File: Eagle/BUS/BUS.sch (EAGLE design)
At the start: 10 parts

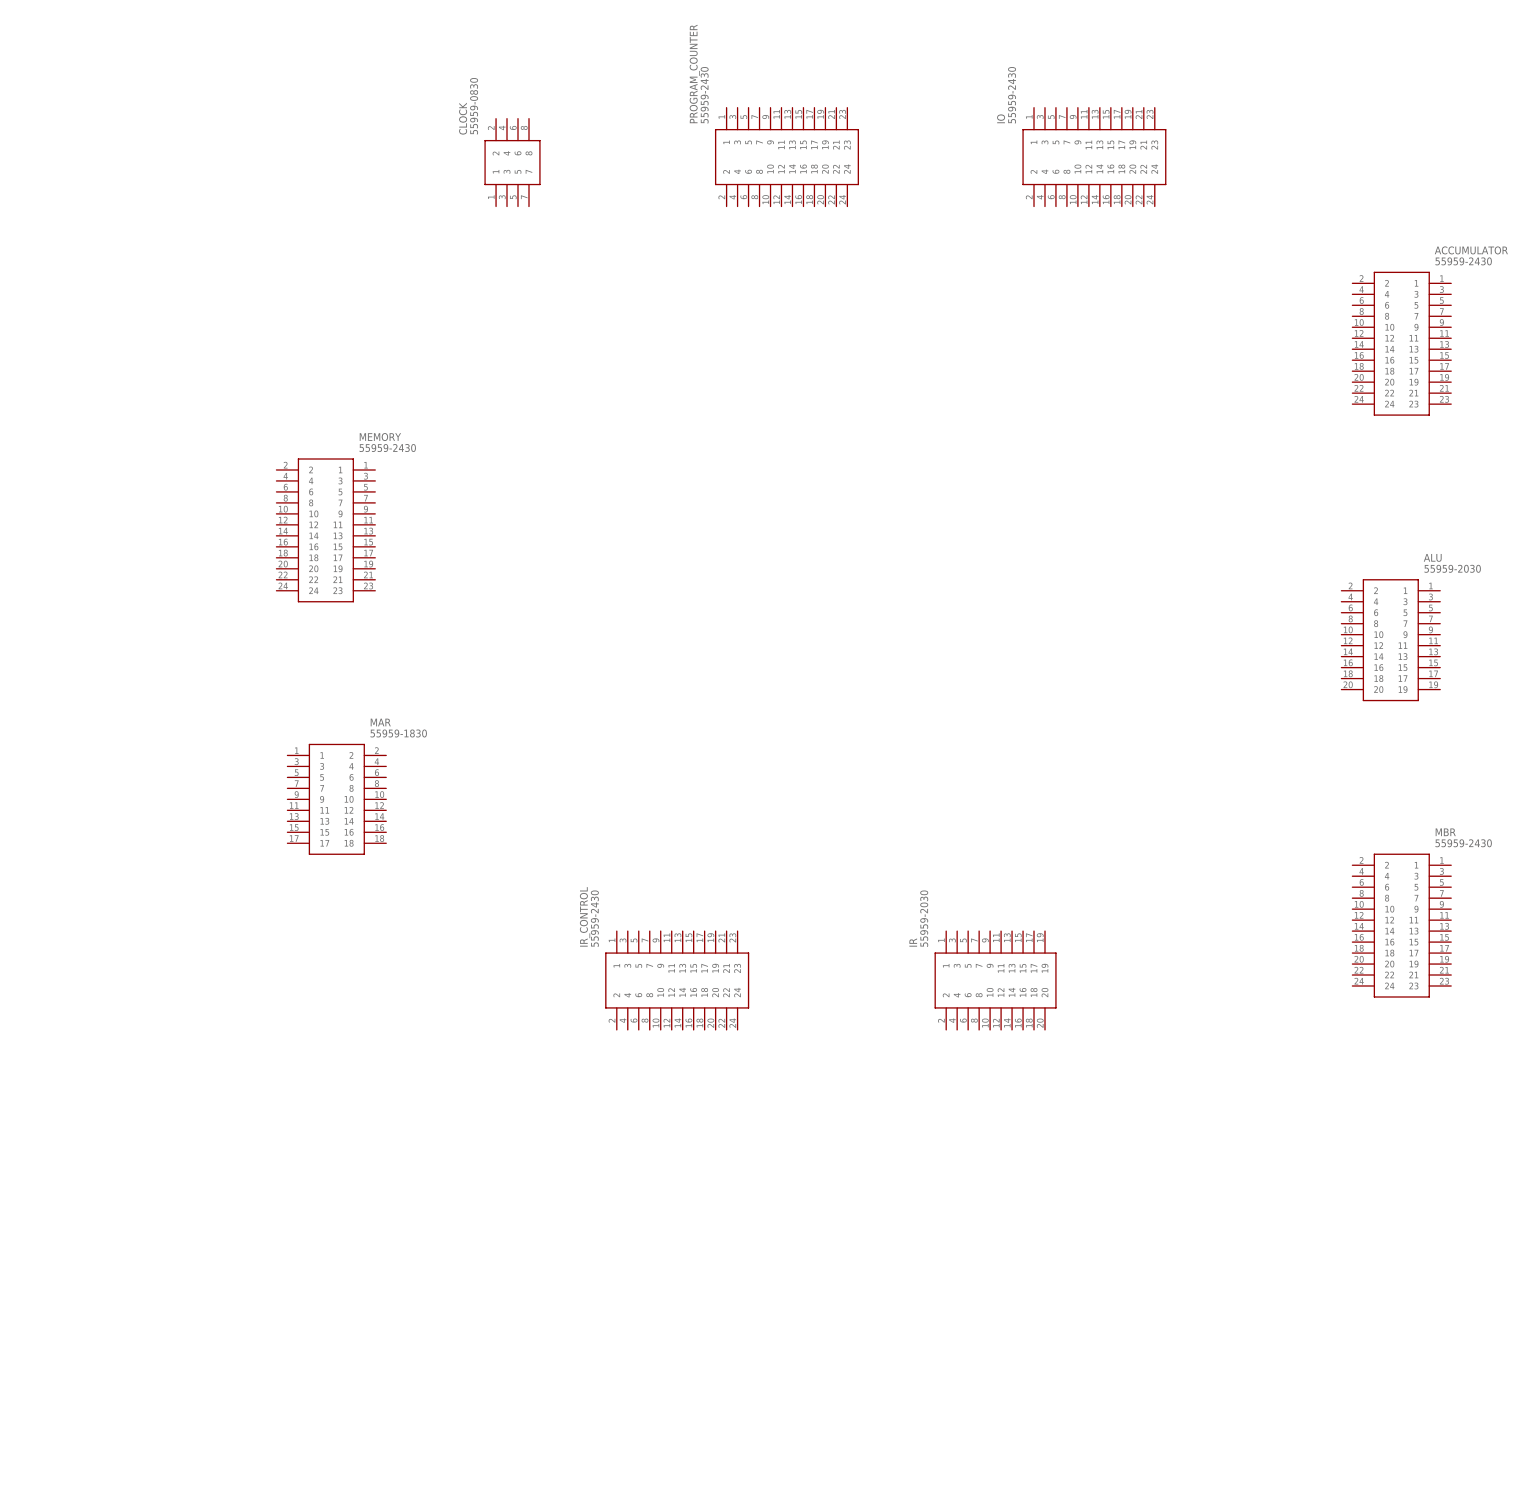
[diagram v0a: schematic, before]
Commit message: added BUS
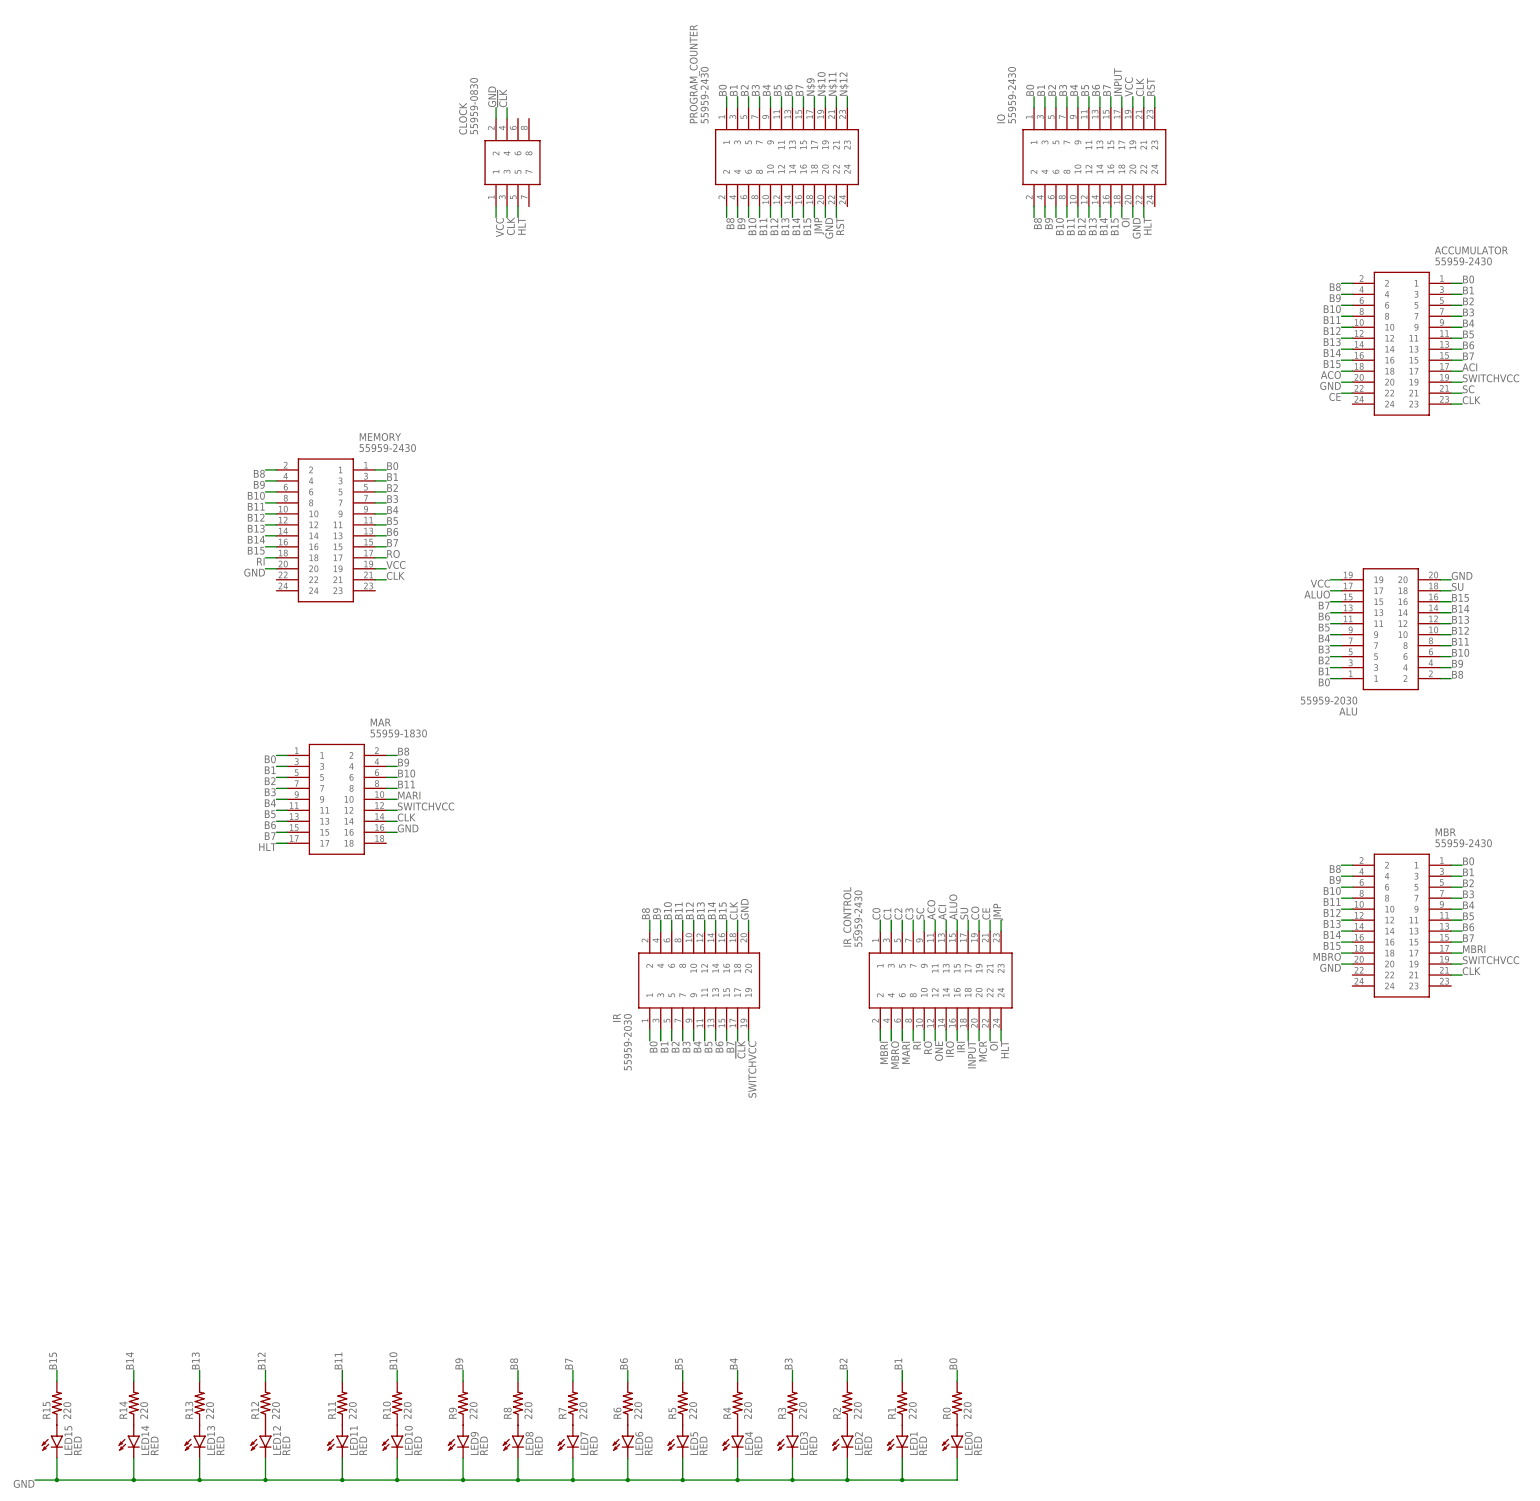
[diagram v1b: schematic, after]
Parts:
- added LED0, LED1, LED10, LED11, LED12, LED13, LED14, LED15, LED2, LED3, LED4, LED5, LED6, LED7, LED8, LED9: RED, led:LED3MM
- added R0, R1, R10, R11, R12, R13, R14, R15, R2, R3, R4, R5, R6, R7, R8, R9: 220, rcl:R-US_0204/7
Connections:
- new net !CLK: CLOCK.4, IR.17
- new net ACI: ACCUMULATOR.17, IR_CONTROL.13
- new net ACO: ACCUMULATOR.18, IR_CONTROL.11
- new net ALUO: ALU.17, IR_CONTROL.15
- new net B0: ACCUMULATOR.1, ALU.1, IO.1, IR.1, MAR.1, MBR.1, MEMORY.1, PROGRAM_COUNTER.1, R0.2
- new net B1: ACCUMULATOR.3, ALU.3, IO.3, IR.3, MAR.3, MBR.3, MEMORY.3, PROGRAM_COUNTER.3, R1.2
- new net B10: ACCUMULATOR.6, ALU.6, IO.6, IR.6, MAR.6, MBR.6, MEMORY.6, PROGRAM_COUNTER.6, R10.2
- new net B11: ACCUMULATOR.8, ALU.8, IO.8, IR.8, MAR.8, MBR.8, MEMORY.8, PROGRAM_COUNTER.8, R11.2
- new net B12: ACCUMULATOR.10, ALU.10, IO.10, IR.10, MBR.10, MEMORY.10, PROGRAM_COUNTER.10, R12.2
- new net B13: ACCUMULATOR.12, ALU.12, IO.12, IR.12, MBR.12, MEMORY.12, PROGRAM_COUNTER.12, R13.2
- new net B14: ACCUMULATOR.14, ALU.14, IO.14, IR.14, MBR.14, MEMORY.14, PROGRAM_COUNTER.14, R14.2
- new net B15: ACCUMULATOR.16, ALU.16, IO.16, IR.16, MBR.16, MEMORY.16, PROGRAM_COUNTER.16, R15.2
- new net B2: ACCUMULATOR.5, ALU.5, IO.5, IR.5, MAR.5, MBR.5, MEMORY.5, PROGRAM_COUNTER.5, R2.2
- new net B3: ACCUMULATOR.7, ALU.7, IO.7, IR.7, MAR.7, MBR.7, MEMORY.7, PROGRAM_COUNTER.7, R3.2
- new net B4: ACCUMULATOR.9, ALU.9, IO.9, IR.9, MAR.9, MBR.9, MEMORY.9, PROGRAM_COUNTER.9, R4.2
- new net B5: ACCUMULATOR.11, ALU.11, IO.11, IR.11, MAR.11, MBR.11, MEMORY.11, PROGRAM_COUNTER.11, R5.2
- new net B6: ACCUMULATOR.13, ALU.13, IO.13, IR.13, MAR.13, MBR.13, MEMORY.13, PROGRAM_COUNTER.13, R6.2
- new net B7: ACCUMULATOR.15, ALU.15, IO.15, IR.15, MAR.15, MBR.15, MEMORY.15, PROGRAM_COUNTER.15, R7.2
- new net B8: ACCUMULATOR.2, ALU.2, IO.2, IR.2, MAR.2, MBR.2, MEMORY.2, PROGRAM_COUNTER.2, R8.2
- new net B9: ACCUMULATOR.4, ALU.4, IO.4, IR.4, MAR.4, MBR.4, MEMORY.4, PROGRAM_COUNTER.4, R9.2
- new net C0: IR_CONTROL.1
- new net C1: IR_CONTROL.3
- new net C2: IR_CONTROL.5
- new net C3: IR_CONTROL.7
- new net CE: ACCUMULATOR.22, IR_CONTROL.21
- new net CLK: ACCUMULATOR.23, CLOCK.3, IO.21, IR.18, MAR.14, MBR.21, MEMORY.21
- new net CO: IR_CONTROL.19
- new net GND: ACCUMULATOR.20, ALU.20, CLOCK.2, IO.20, IR.20, LED0.C, LED1.C, LED10.C, LED11.C, LED12.C, LED13.C, LED14.C, LED15.C, LED2.C, LED3.C, LED4.C, LED5.C, LED6.C, LED7.C, LED8.C, LED9.C, MAR.16, MBR.20, MEMORY.20, PROGRAM_COUNTER.20
- new net HLT: CLOCK.5, IO.22, IR_CONTROL.24, MAR.17
- new net INPUT: IO.17, IR_CONTROL.18
- new net IRI: IR_CONTROL.16
- new net IRO: IR_CONTROL.14
- new net JMP: IR_CONTROL.23, PROGRAM_COUNTER.18
- new net MARI: IR_CONTROL.6, MAR.10
- new net MBRI: IR_CONTROL.2, MBR.17
- new net MBRO: IR_CONTROL.4, MBR.18
- new net MCR: IR_CONTROL.20
- new net N$1: LED1.A, R1.1
- new net N$10: PROGRAM_COUNTER.19
- new net N$11: PROGRAM_COUNTER.21
- new net N$12: PROGRAM_COUNTER.23
- new net N$13: LED9.A, R9.1
- new net N$14: LED10.A, R10.1
- new net N$15: LED11.A, R11.1
- new net N$16: LED12.A, R12.1
- new net N$17: LED13.A, R13.1
- new net N$18: LED14.A, R14.1
- new net N$19: LED15.A, R15.1
- new net N$2: LED2.A, R2.1
- new net N$20: LED0.A, R0.1
- new net N$3: LED3.A, R3.1
- new net N$4: LED4.A, R4.1
- new net N$5: LED5.A, R5.1
- new net N$6: LED6.A, R6.1
- new net N$7: LED7.A, R7.1
- new net N$8: LED8.A, R8.1
- new net N$9: PROGRAM_COUNTER.17
- new net OI: IO.18, IR_CONTROL.22
- new net ONE: IR_CONTROL.12
- new net RI: IR_CONTROL.8, MEMORY.18
- new net RO: IR_CONTROL.10, MEMORY.17
- new net RST: IO.23, PROGRAM_COUNTER.22
- new net SC: ACCUMULATOR.21, IR_CONTROL.9
- new net SU: ALU.18, IR_CONTROL.17
- new net SWITCHVCC: ACCUMULATOR.19, IR.19, MAR.12, MBR.19
- new net VCC: ALU.19, CLOCK.1, IO.19, MEMORY.19
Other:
- moved on the sheet: ALU, IR, IR_CONTROL

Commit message: added pull down resistors and reset circuit to BUS
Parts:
- added OR_GATE: SN74HC32N, SamacSys_Parts:SN74HC32N
- added PD0, PD1, PD10, PD11, PD12, PD13, PD14, PD15, PD2, PD3, PD4, PD5, PD6, PD7, PD8, PD9: 10k, rcl:R-US_0204/7
- added RESET: MHPS2273N, SamacSys_Parts:MHPS2273N
- added RST_RELAY: SRD-05VDC-SL-C, SamacSys_Parts:SRD-05VDC-SL-C
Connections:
- removed net N$10: PROGRAM_COUNTER.19
- removed net N$12: PROGRAM_COUNTER.23
- removed net N$9: PROGRAM_COUNTER.17
- new net !RST: PROGRAM_COUNTER.22, RESET.COM_1
- new net AC_CE: ACCUMULATOR.22, OR_GATE.1A
- new net CL_CE: IR_CONTROL.21, OR_GATE.1B
- new net CL_HLT: IR_CONTROL.24, OR_GATE.2B
- new net IO_HLT: IO.22, OR_GATE.3B
- new net MAR_HLT: MAR.17, OR_GATE.2A
- net B0: now also PD0.2
- net B1: now also PD1.2
- net B10: now also PD10.2
- net B11: now also PD11.2
- net B12: now also PD12.2
- net B13: now also PD13.2
- net B14: now also PD14.2
- net B15: now also PD15.2
- net B2: now also PD2.2
- net B3: now also PD3.2
- net B4: now also PD4.2
- net B5: now also PD5.2
- net B6: now also PD6.2
- net B7: now also PD7.2
- net B8: now also PD8.2
- net B9: now also PD9.2
- net CE: now also OR_GATE.1Y, PROGRAM_COUNTER.23; no longer ACCUMULATOR.22, IR_CONTROL.21
- net CLK: now also PROGRAM_COUNTER.21
- net CO: now also PROGRAM_COUNTER.17
- net GND: now also OR_GATE.4A, OR_GATE.4B, OR_GATE.GND, PD0.1, PD1.1, PD10.1, PD11.1, PD12.1, PD13.1, PD14.1, PD15.1, PD2.1, PD3.1, PD4.1, PD5.1, PD6.1, PD7.1, PD8.1, PD9.1, RESET.N.O._1, RST_RELAY.3
- net HLT: now also OR_GATE.3Y; no longer IO.22, IR_CONTROL.24, MAR.17
- net N$11: now also OR_GATE.2Y, OR_GATE.3A; no longer PROGRAM_COUNTER.21
- net RST: now also RESET.N.O._2, RST_RELAY.2; no longer PROGRAM_COUNTER.22
- net SWITCHVCC: now also RST_RELAY.1
- net VCC: now also OR_GATE.VCC, PROGRAM_COUNTER.19, RESET.COM_2, RESET.N.C._1, RST_RELAY.5

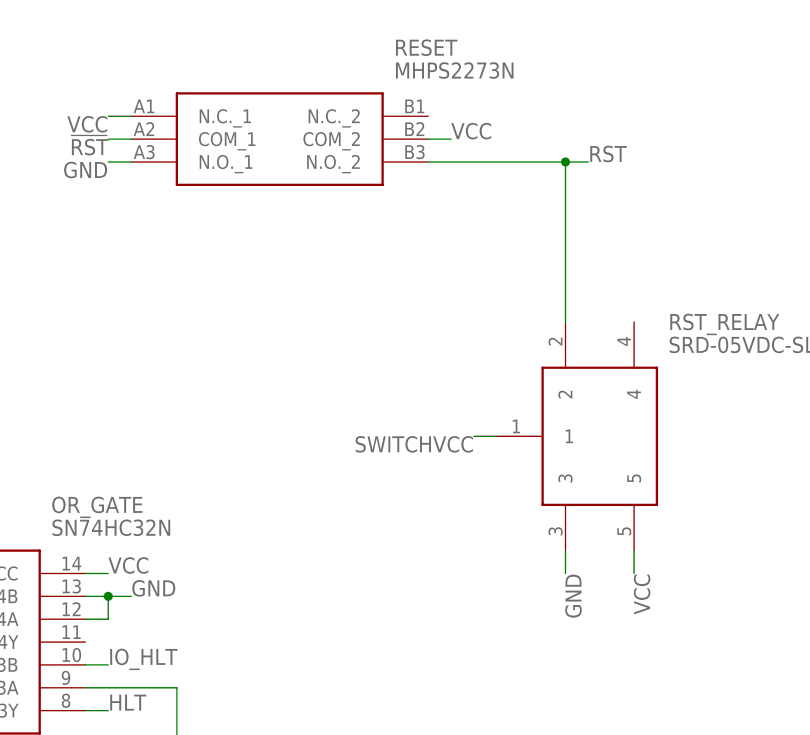
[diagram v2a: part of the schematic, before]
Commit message: added flyback diode
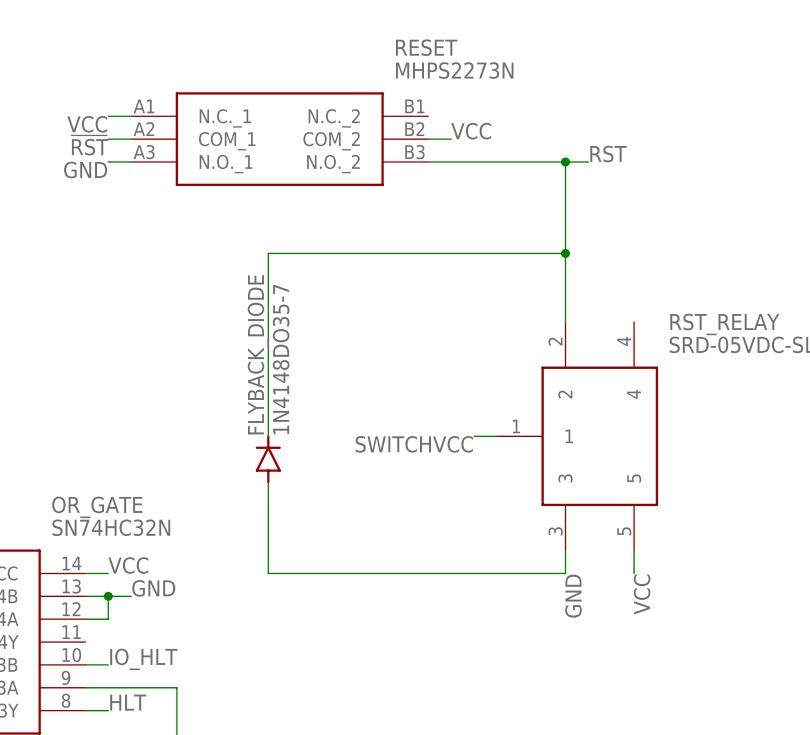
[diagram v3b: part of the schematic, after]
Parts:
- added FLYBACK_DIODE: 1N4148DO35-7, diode:1N4148DO35-7
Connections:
- net GND: now also FLYBACK_DIODE.A
- net RST: now also FLYBACK_DIODE.C
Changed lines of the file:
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@@
 <layer number="97" name="Info" color="7" fill="1" visible="yes" active="yes"/>
 <layer number="98" name="Guide" color="6" fill="1" visible="yes" active="yes"/>
+<layer number="99" name="SpiceOrder" color="5" fill="1" visible="yes" active="yes"/>
 </layers>
 <schematic xreflabel="%F%N/%S.%C%R" xrefpart="/%S.%C%R">
@@
 <part name="PD15" library="rcl" library_urn="urn:adsk.eagle:library:334" deviceset="R-US_" device="0204/7" package3d_urn="urn:adsk.eagle:package:23498/2" value="10k"/>
 <part name="OR_GATE" library="SamacSys_Parts" deviceset="SN74HC32N" device=""/>
+<part name="FLYBACK_DIODE" library="diode" library_urn="urn:adsk.eagle:library:210" deviceset="1N4148" device="DO35-7" package3d_urn="urn:adsk.eagle:package:43339/2"/>
 </parts>
 <sheets>
@@
 <attribute name="NAME" x="57.15" y="124.46" size="1.778" layer="95" align="center-left"/>
 <attribute name="VALUE" x="57.15" y="121.92" size="1.778" layer="96" align="center-left"/>
+</instance>
+<instance part="FLYBACK_DIODE" gate="G$1" x="81.28" y="129.54" smashed="yes" rot="R90">
+<attribute name="NAME" x="80.7974" y="132.08" size="1.778" layer="95" rot="R90"/>
+<attribute name="VALUE" x="83.5914" y="132.08" size="1.778" layer="96" rot="R90"/>
 </instance>
 </instances>
@@
 <wire x1="114.3" y1="119.38" x2="114.3" y2="116.84" width="0.1524" layer="91"/>
 <label x="114.3" y="116.84" size="1.778" layer="95" rot="R270"/>
+<wire x1="114.3" y1="116.84" x2="81.28" y2="116.84" width="0.1524" layer="91"/>
+<pinref part="FLYBACK_DIODE" gate="G$1" pin="A"/>
+<wire x1="81.28" y1="116.84" x2="81.28" y2="127" width="0.1524" layer="91"/>
 </segment>
 <segment>
@@
 <wire x1="99.06" y1="162.56" x2="114.3" y2="162.56" width="0.1524" layer="91"/>
 <pinref part="RST_RELAY" gate="G$1" pin="2"/>
-<wire x1="114.3" y1="162.56" x2="114.3" y2="144.78" width="0.1524" layer="91"/>
+<wire x1="114.3" y1="162.56" x2="114.3" y2="152.4" width="0.1524" layer="91"/>
+<wire x1="114.3" y1="152.4" x2="114.3" y2="144.78" width="0.1524" layer="91"/>
 <wire x1="114.3" y1="162.56" x2="116.84" y2="162.56" width="0.1524" layer="91"/>
 <junction x="114.3" y="162.56"/>
 <label x="116.84" y="162.56" size="1.778" layer="95"/>
-</segment>
-</net>
+<pinref part="FLYBACK_DIODE" gate="G$1" pin="C"/>
+<wire x1="81.28" y1="132.08" x2="81.28" y2="152.4" width="0.1524" layer="91"/>
+<wire x1="81.28" y1="152.4" x2="114.3" y2="152.4" width="0.1524" layer="91"/>
+<junction x="114.3" y="152.4"/>
+</segment>
+</net>
